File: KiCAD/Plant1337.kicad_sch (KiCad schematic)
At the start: 43 parts, among them Q1 AO3400A, Q2 AO3400A, Q3 AO3400A, Q4 AO3400A, U1 SHTC3

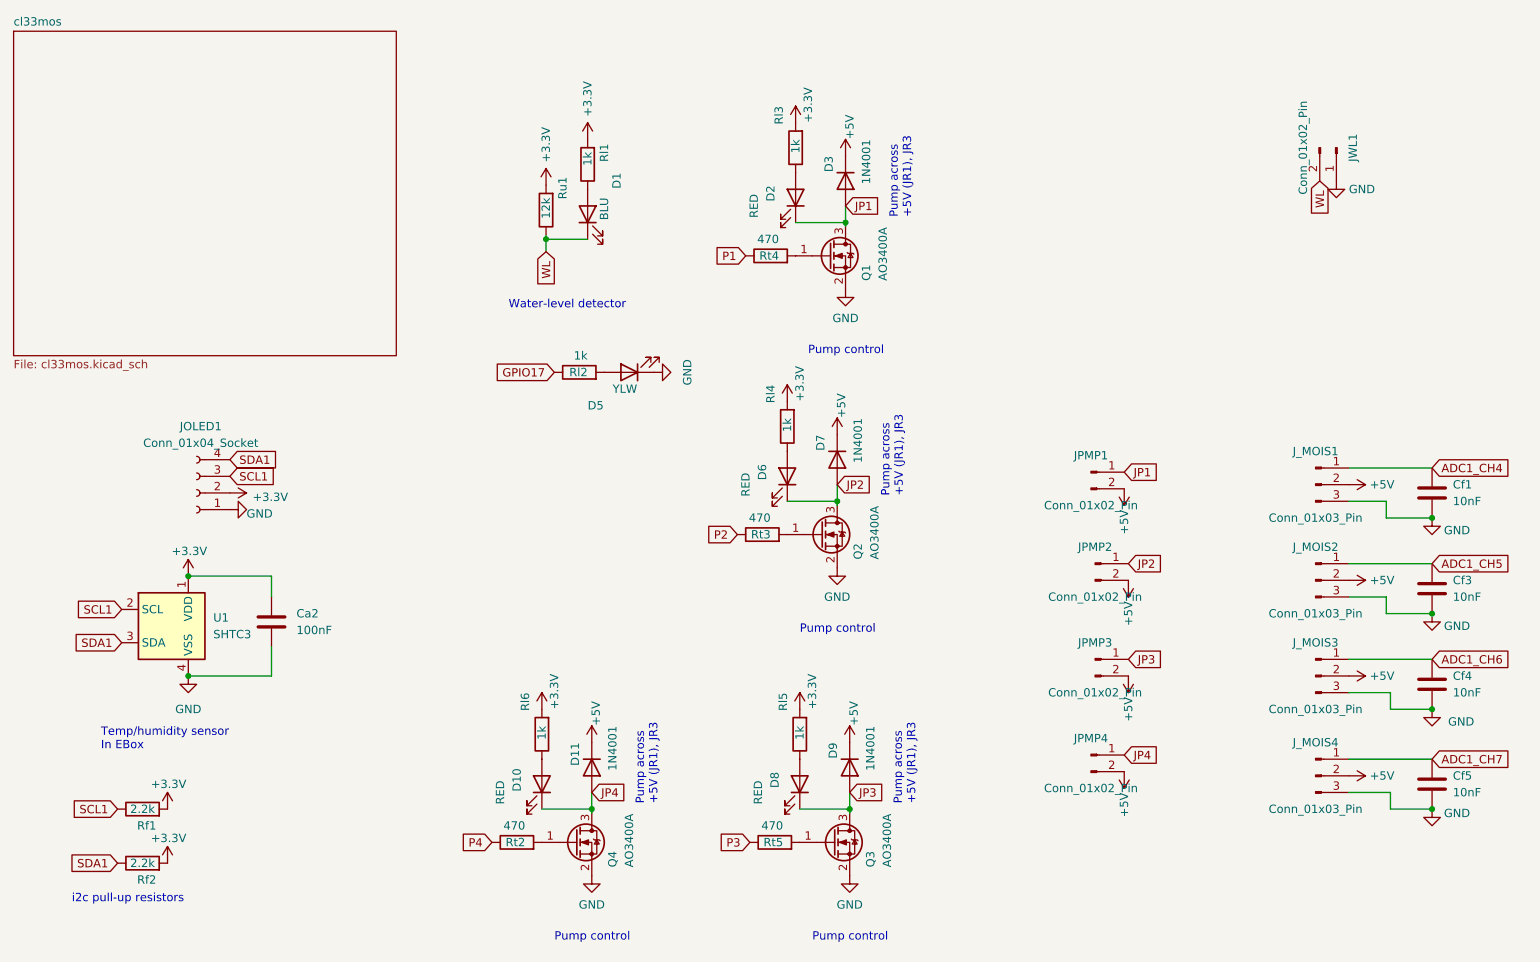
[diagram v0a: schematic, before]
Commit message: Version 1.0.0 (#42)
### Added
- **Hardware Board v2.x & ESP32-S3 Support**: Added PlatformIO configurations (`esp32s3`, `usb_s3`, `wifi_s3`), `BOARD_V20` pin mappings for `ESP32-S3-WROOM-1-N8R2` with USB-C, updated KiCAD schematics/PCB layouts (v2.0–v2.2 with boot/reset push-buttons and improved flyback diode placement), and BOM (`KiCAD/Plant133.csv`).
- **3D-Printed Enclosure & Accessories**:
  - Updated EBox (`scad/box/`) for Board v2.1+ and added OLED support bracket (`OLEDSupport.scad`) and board test fixture (`fixture.scad`).
  - Added reservoir cover/cap (`scad/reservoir_cover/`) with cutouts for the EBox, tubing, and wires.
  - Updated reservoir insert (`scad/reservoir_insert/`) and extracted reusable vitamin models (`vertical_pump.scad`, `float.scad`).
  - Updated solder stencil fixture and added stencil edge-support frame (`scad/stencil_fixture/`).
- **Adafruit IO & SSL/TLS MQTT Support**: Added NTP time synchronization (`og3::Ntp`), SSL/TLS with optional certificate verification, and Adafruit IO MQTT mode with feed filtering/rate-limiting in both firmware and the Svelte MQTT configuration UI.
- **System Status Versioning**: Exposed `software` and `hardware` version fields in `GET /api/status`.
- **Native Unit Tests & Dependabot**: Ported unit tests (`test/test_watering/test_watering.cpp`) to `og3` under `[env:native]`, enabled `pio test -e native` in `util/check.sh`, and added GitHub Actions Dependabot configuration.

### Changed
- **Framework Upgrade**: Upgraded to **og3 v0.7.0**, **og3x-oled v0.6.1**, and **og3x-shtc3 v0.6.0**, linking modules by pointer via `require(...)` and making `DoseLog` an `og3::Module`.
- **Web UI & API Alignment**: Updated Svelte WiFi and MQTT configuration pages to use `og3` variable keys (`essId`, `wifiPassword`, `hostAddr`, `authUser`, `authPassword`) and updated `build-svelte.sh` to use `--etag=always`.
- **MQTT Optimization**: Avoided sending duplicate reservoir status updates per plant.

### Fixed
- **Plant API Validation*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
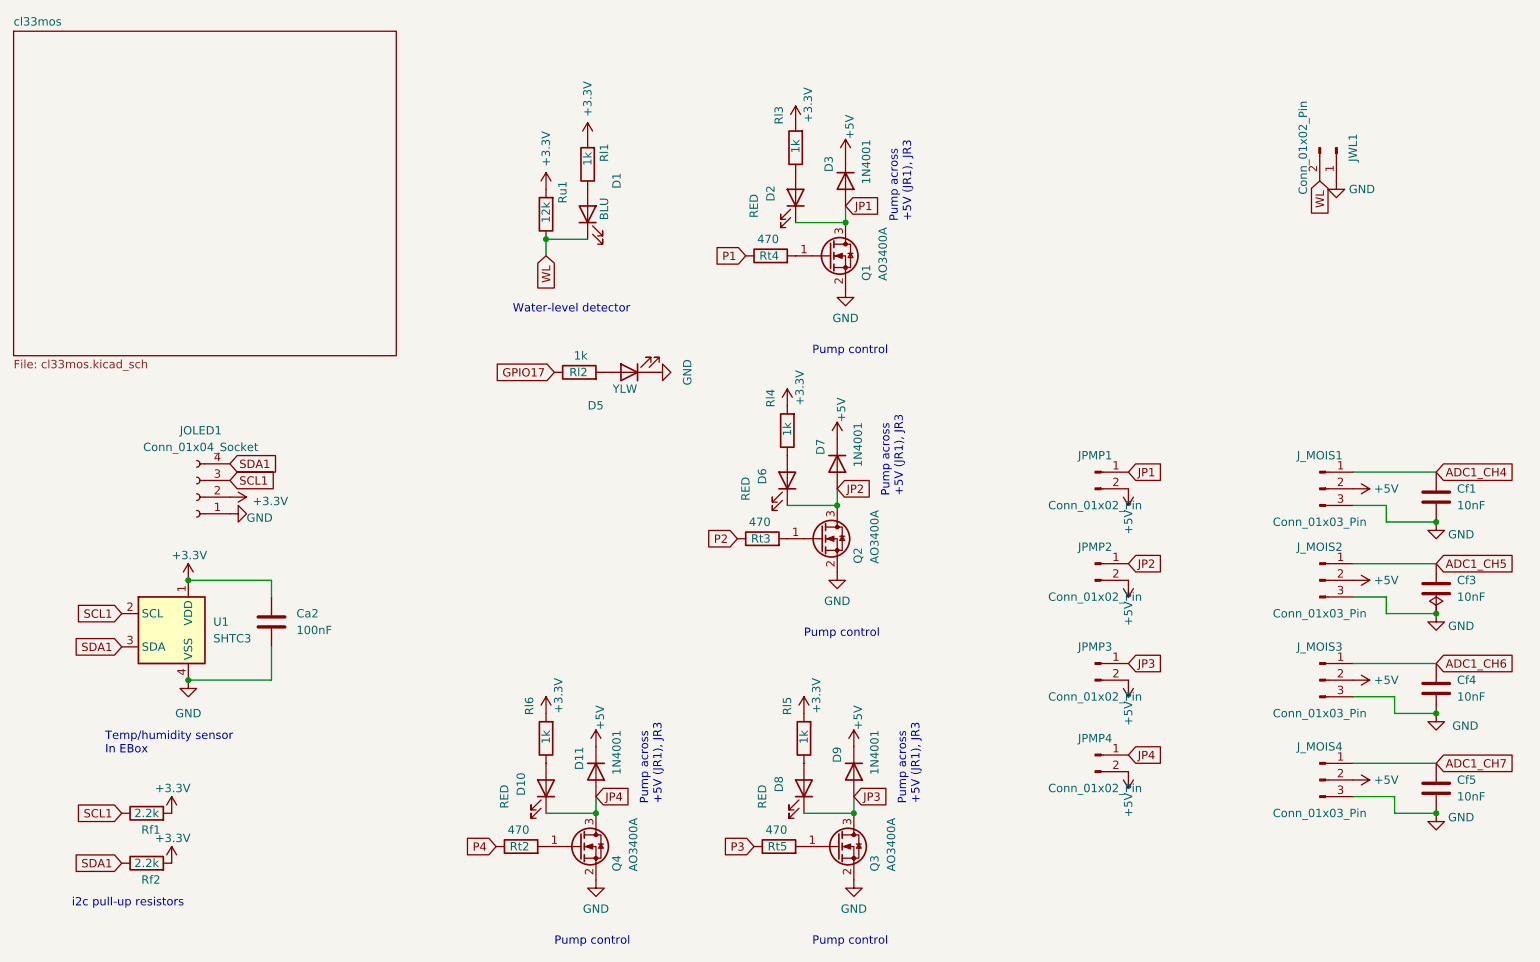
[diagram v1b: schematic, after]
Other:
- moved on the sheet: Cf1, Cf3, Cf4, Cf5, D10, D11, D6, D7, D8, D9, JOLED1, JPMP1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
